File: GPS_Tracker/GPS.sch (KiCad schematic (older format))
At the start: 3 parts

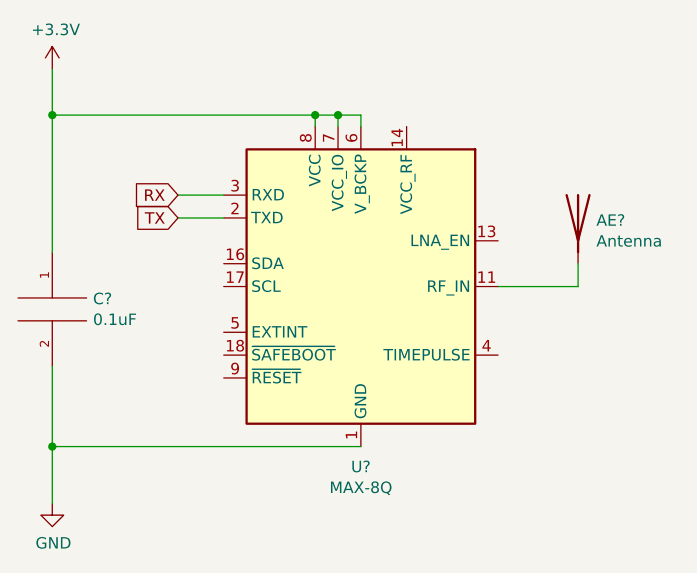
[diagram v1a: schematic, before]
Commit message: added hichary labels
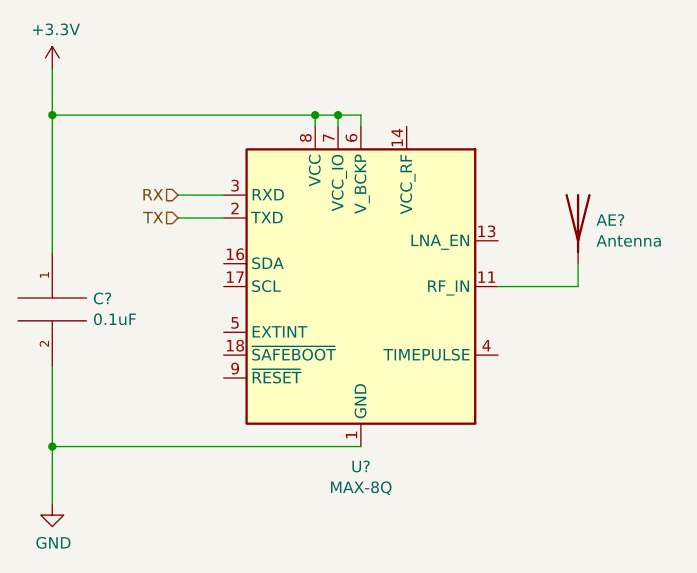
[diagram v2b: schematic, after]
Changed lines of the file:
@@
 	1    0    0    -1
 $EndComp
-Text GLabel 4950 3050 0    50   Input ~ 0
-RX
-Text GLabel 4950 3150 0    50   Input ~ 0
-TX
 Wire Wire Line
 	4950 3150 5150 3150
@@
 	5750 2700 5650 2700
 Connection ~ 5650 2700
+Text HLabel 4950 3150 0    50   Input ~ 0
+TX
+Text HLabel 4950 3050 0    50   Input ~ 0
+RX
 $EndSCHEMATC
